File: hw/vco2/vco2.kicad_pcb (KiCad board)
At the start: 4 copper layers, 60 x 110 mm, 136 parts, among them J1 Conn_02x08_Odd_Even, Q1 DNP, U1 SSI2131, U2 TL431BCDBZ, U3 TL072HxD, U4 TL072HxD, U5 TL072HxD, U6 TL431BCDBV, U7 TL072HxD, U8 TL072HxD, U9 SSI2131

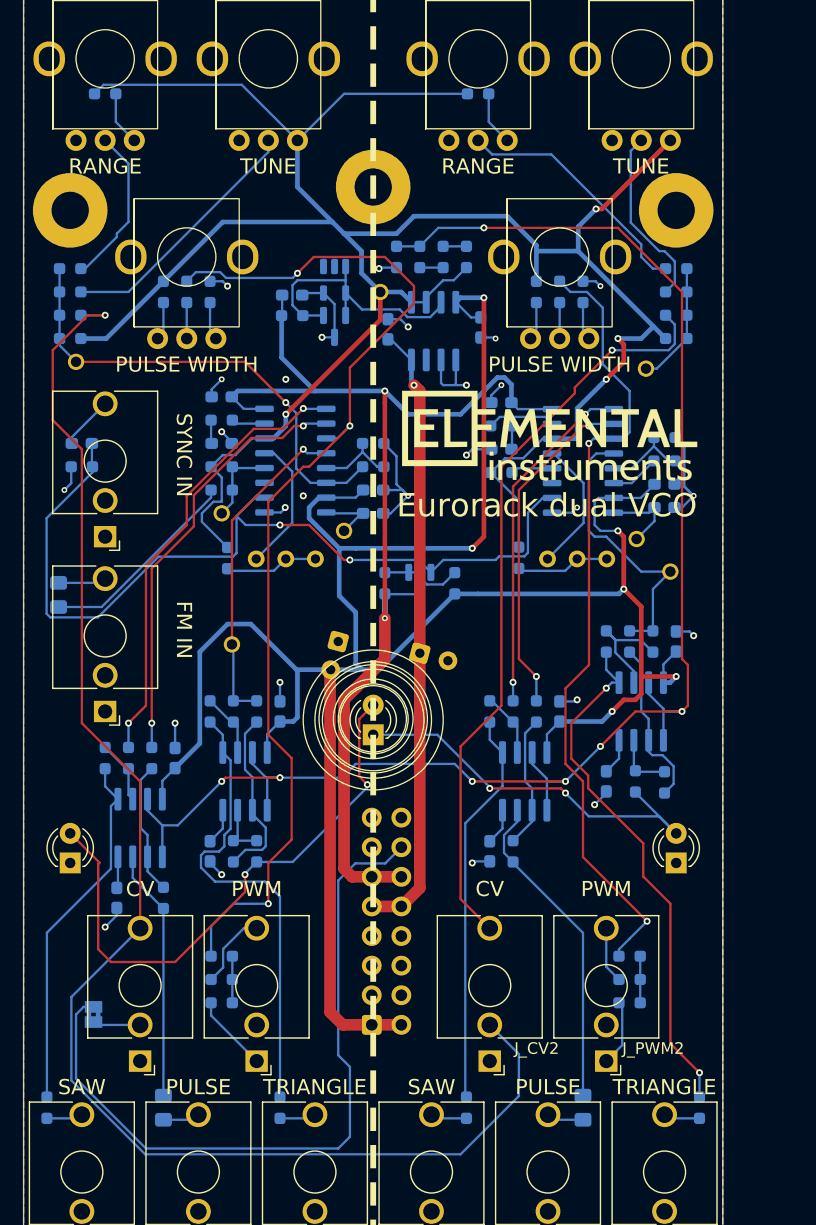
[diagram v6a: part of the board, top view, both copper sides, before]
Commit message: Clean up VCO board, reduce to 2 layers
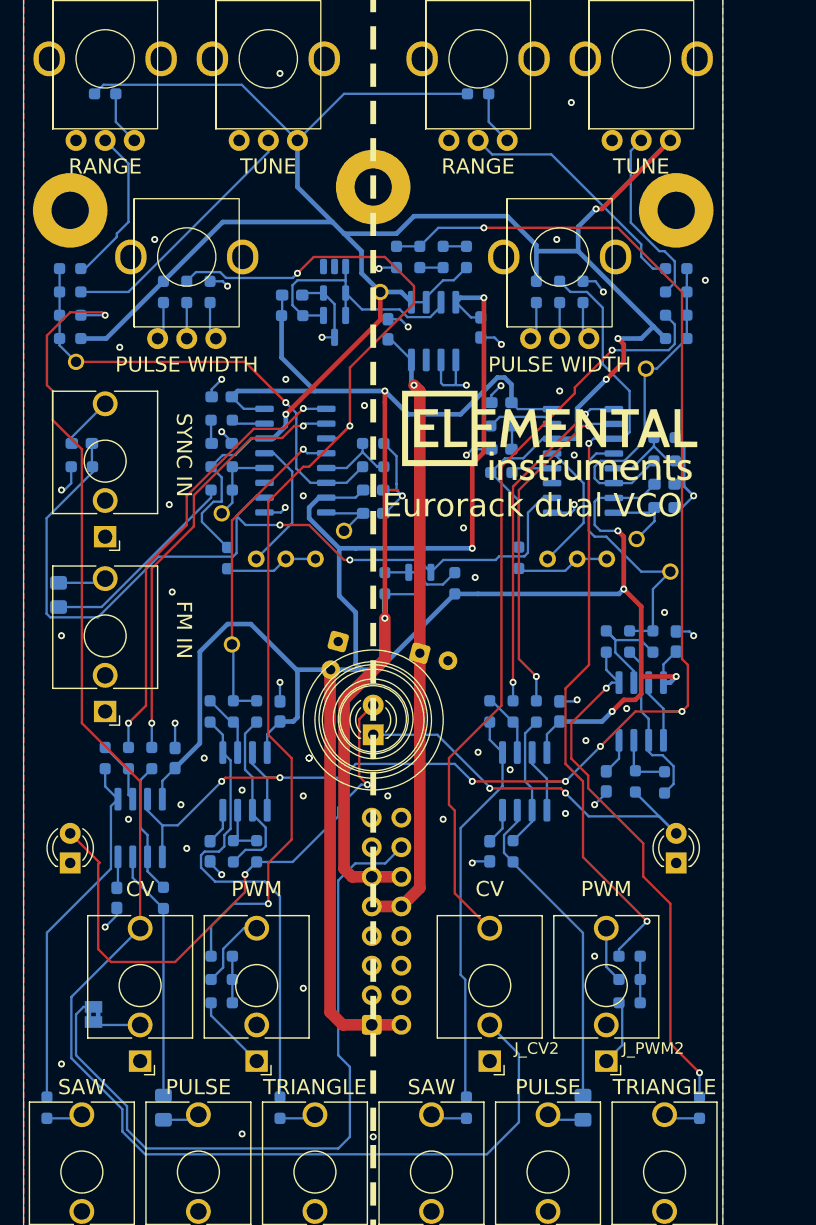
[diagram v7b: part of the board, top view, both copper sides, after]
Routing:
- net /EXPO_FREQ2: track 14.8 -> 29.1 mm
- net Net-(J_CV1-PadT): track 126.3 -> 129.2 mm
- net Net-(J_CV2-PadT): track 64.4 -> 65.2 mm
- net GND: vias 26 -> 61
- removed copper zone on In1.Cu, net GND
- removed copper zone on In2.Cu, net GND
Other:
- copper layers 4 -> 2

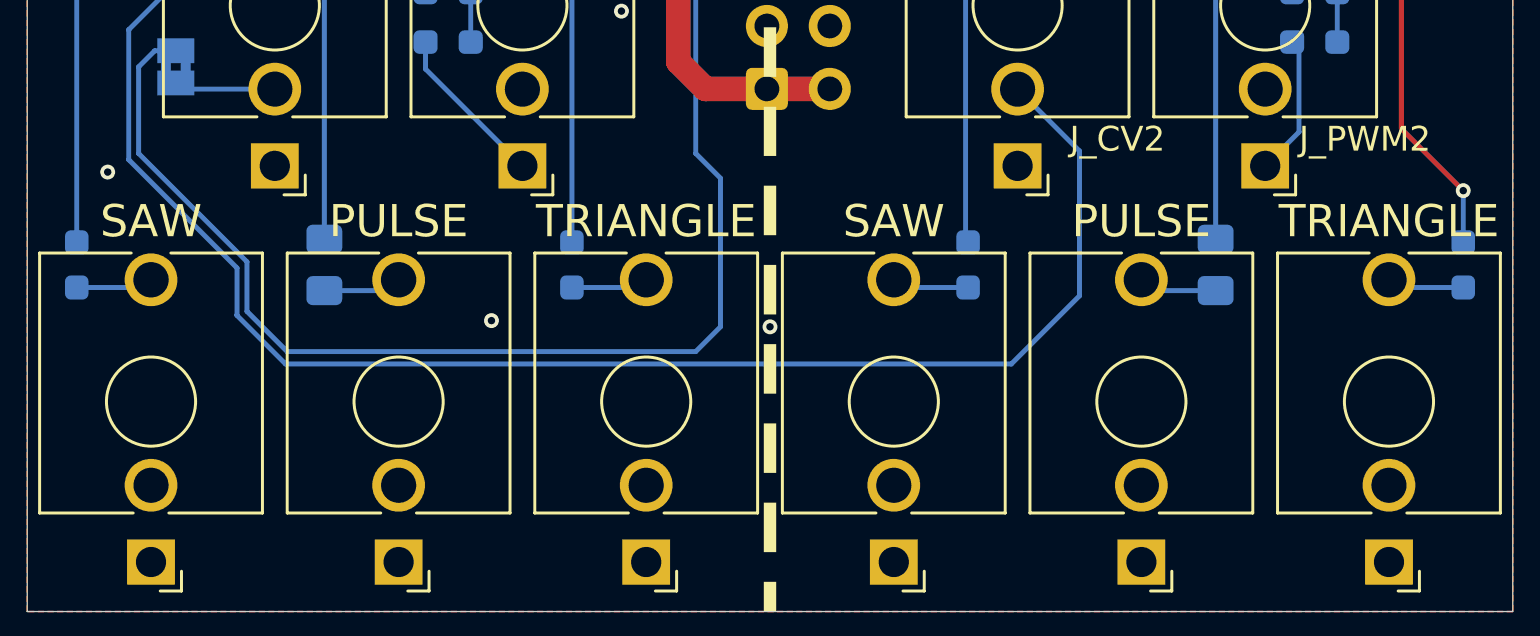
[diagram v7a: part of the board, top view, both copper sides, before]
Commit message: Add normalisation on outputs
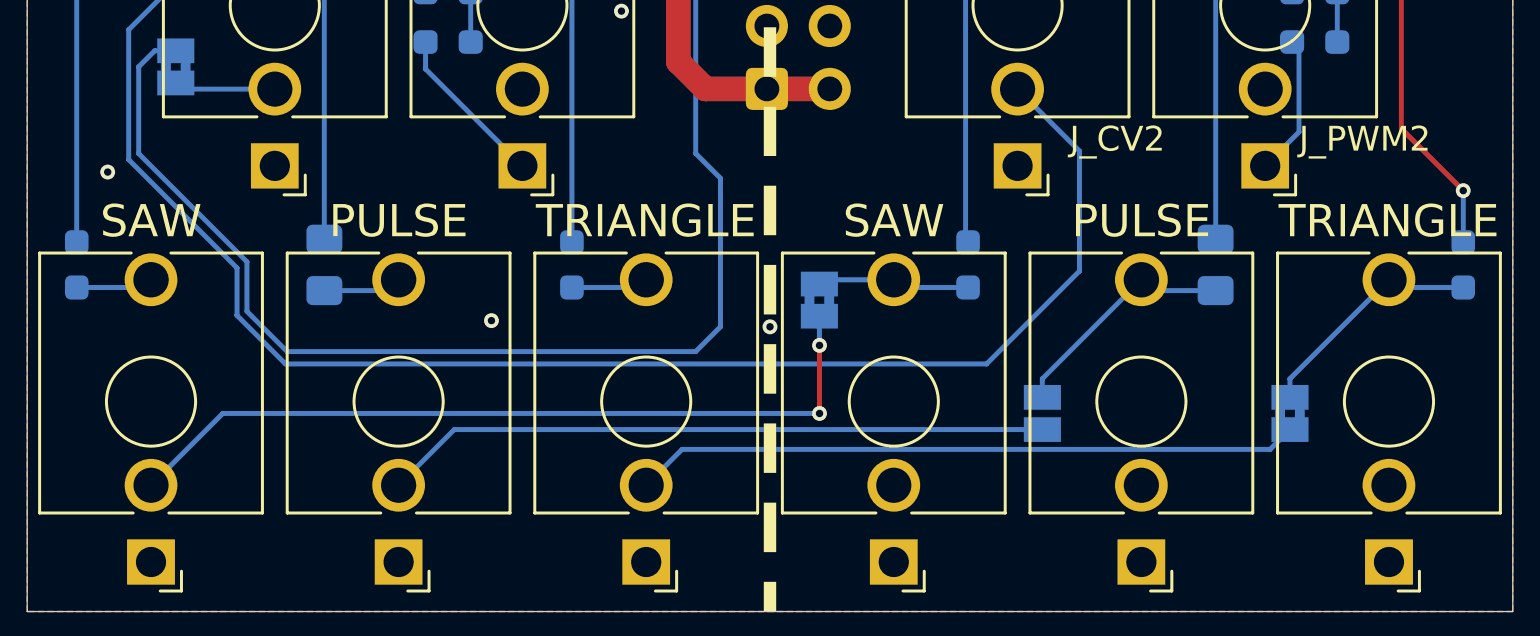
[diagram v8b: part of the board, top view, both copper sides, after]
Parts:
- added JP2: jumper, Jumper:SolderJumper-2_P1.3mm_Bridged2Bar_Pad1.0x1.5mm, B.Cu at (112.0, 137.4)
- added JP3: jumper, Jumper:SolderJumper-2_P1.3mm_Open_Pad1.0x1.5mm, B.Cu at (121.0, 142.0)
- added JP4: jumper, Jumper:SolderJumper-2_P1.3mm_Bridged2Bar_Pad1.0x1.5mm, B.Cu at (131.0, 142.0)
- moved G*** 101.2 mm to (109.9, 42.6)
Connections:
- J_PULSE1 pad TN: unconnected-(J_PULSE1-PadTN) -> Net-(JP3-B)
- J_SAW1 pad TN: unconnected-(J_SAW1-PadTN) -> Net-(JP2-B)
- J_TRI1 pad TN: unconnected-(J_TRI1-PadTN) -> Net-(JP4-B)
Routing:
- net Net-(JP2-B): track 0.00 -> 32.1 mm, vias 0 -> 2
- net Net-(JP4-B): track 0.00 -> 26.9 mm
- net Net-(JP3-B): track 0.00 -> 26.9 mm
- net Net-(JP3-A): track 3.18 -> 9.59 mm
- net Net-(JP4-A): track 3.13 -> 9.54 mm
- net Net-(JP2-A): track 3.13 -> 6.21 mm
- net Net-(J_CV1-PadT): track 129.2 -> 128.7 mm
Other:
- board text added: "Dual VCO rev1"
- board text added: "Elemental Instruments Jonas Norling 2026"
- board text removed: "VCO2 rev1 Elemental Instruments Jonas Norling 2026"
